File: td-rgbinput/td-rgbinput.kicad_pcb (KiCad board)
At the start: 2 copper layers, 165 x 50 mm, 121 parts, among them J1 Conn_01x06_Male, J2 Conn_01x07_Male, J3 Conn_01x06_Male, J5 DB15_Female_HighDensity_Mount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, Q1 2N7002NXBKR, Q2 2N7002NXBKR, Q3 2N7002NXBKR, Q4 2N7002NXBKR, Q5 2N7002NXBKR, Q6 2N7002NXBKR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

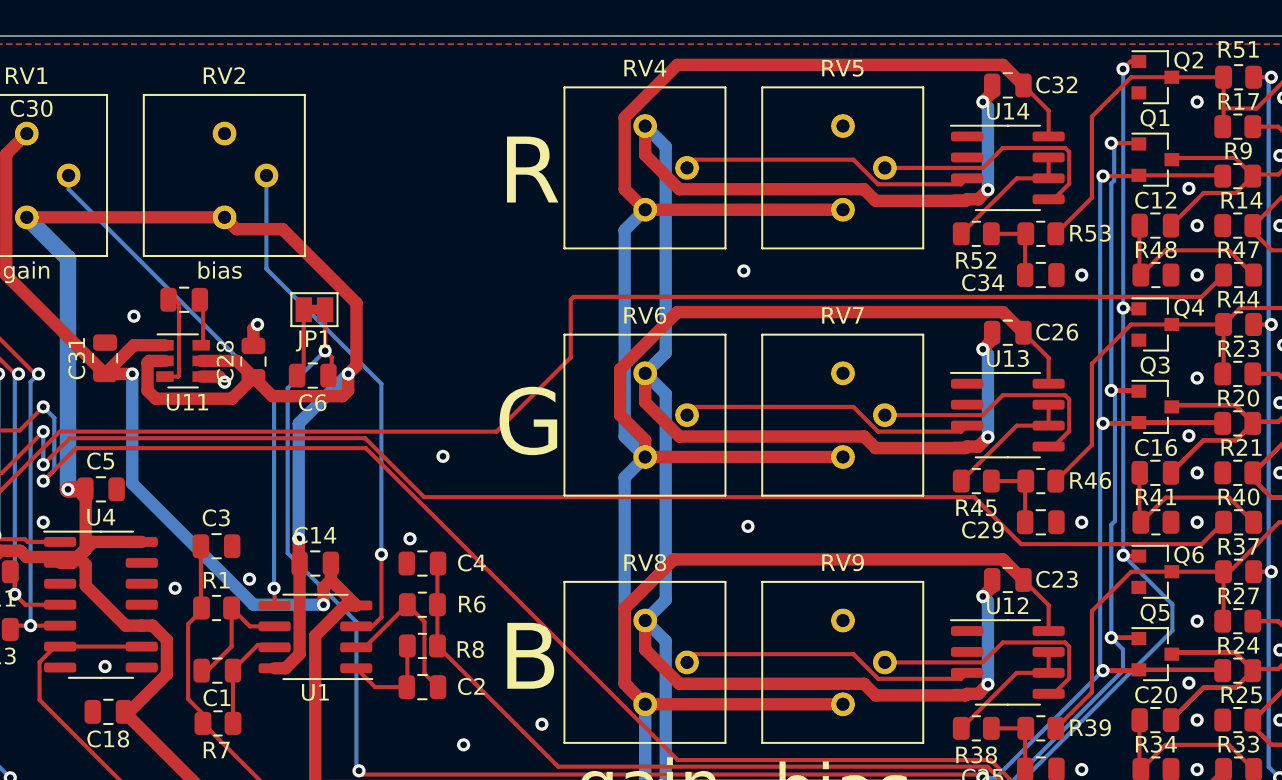
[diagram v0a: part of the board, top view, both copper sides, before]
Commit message: update footprints from kicad 6 library
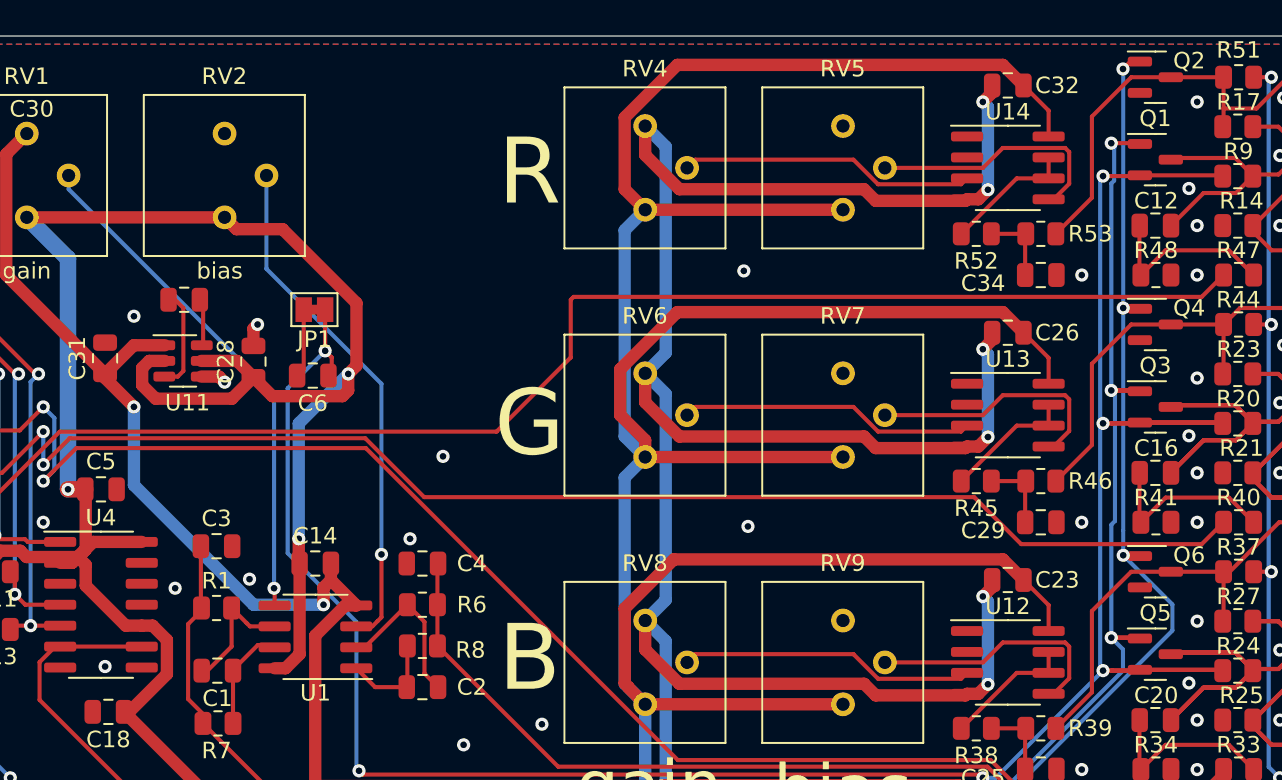
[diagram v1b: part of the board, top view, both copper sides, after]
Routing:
- net -5V: track 334.2 -> 333.2 mm

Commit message: increment version number
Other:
- board text added: "td-rgbinput v1.1 CC0 2021 https://github.com/tdaede/td-crt"
- board text removed: "td-rgbinput v1.0 CC0 2021 https://github.com/tdaede/td-crt"
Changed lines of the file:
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@@
     (effects (font (size 1 1) (thickness 0.15)) (justify right))
   )
-  (gr_text "td-rgbinput v1.0 CC0 2021\nhttps://github.com/tdaede/td-crt" (at 99 98) (layer "F.SilkS")
+  (gr_text "td-rgbinput v1.1 CC0 2021\nhttps://github.com/tdaede/td-crt" (at 99 98) (layer "F.SilkS")
     (effects (font (size 1 1) (thickness 0.15)))
   )
